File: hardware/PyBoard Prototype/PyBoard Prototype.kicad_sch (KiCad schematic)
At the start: 10 parts, among them J1 MIDI In, J2 MIDI Out, Q1 Q_PNP_BCE, U1 PyBoard_v1.1, U2 PC817, U3 MIKROE-506

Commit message: Some more experiments with MicroPython
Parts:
- added D?: D, symbol Device:D
- Q1: value Q_PNP_BCE -> 2N5401
- R2: value 150 -> 100
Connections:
- net +3V3: now also D?.2 (A); no longer R2.2
- new net: D?.1 (K), R2.2
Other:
- note added: "(3.3V - 0.6V) / 100Ohm = 27mA similar to 5V / 220Ohm from the MIDI specs, in case of short-circuit in the cable. However (5V-1.2V)/(2x220Ohm) = 8.6mA While (3V-0.6V-1.2V)/(100Ohm + 220Ohm) = 4.7mA Need to test if this is still sufficient."
- note removed: "3.3V / 150Ohm = 22mA similar to 5V / 220Ohm from the MIDI specs, in case of short-circuit in the cable. However (5V-1.2V)/(2x220Ohm) = 8.6mA While (3V-1.2v)/(150Ohm + 220Ohm) = 5.6mA Need to test if this is still sufficient. Otherwise 30Ohm would come close but draw 110mA in case of a short-circuit!"
- moved on the sheet: J2, Q1, R2

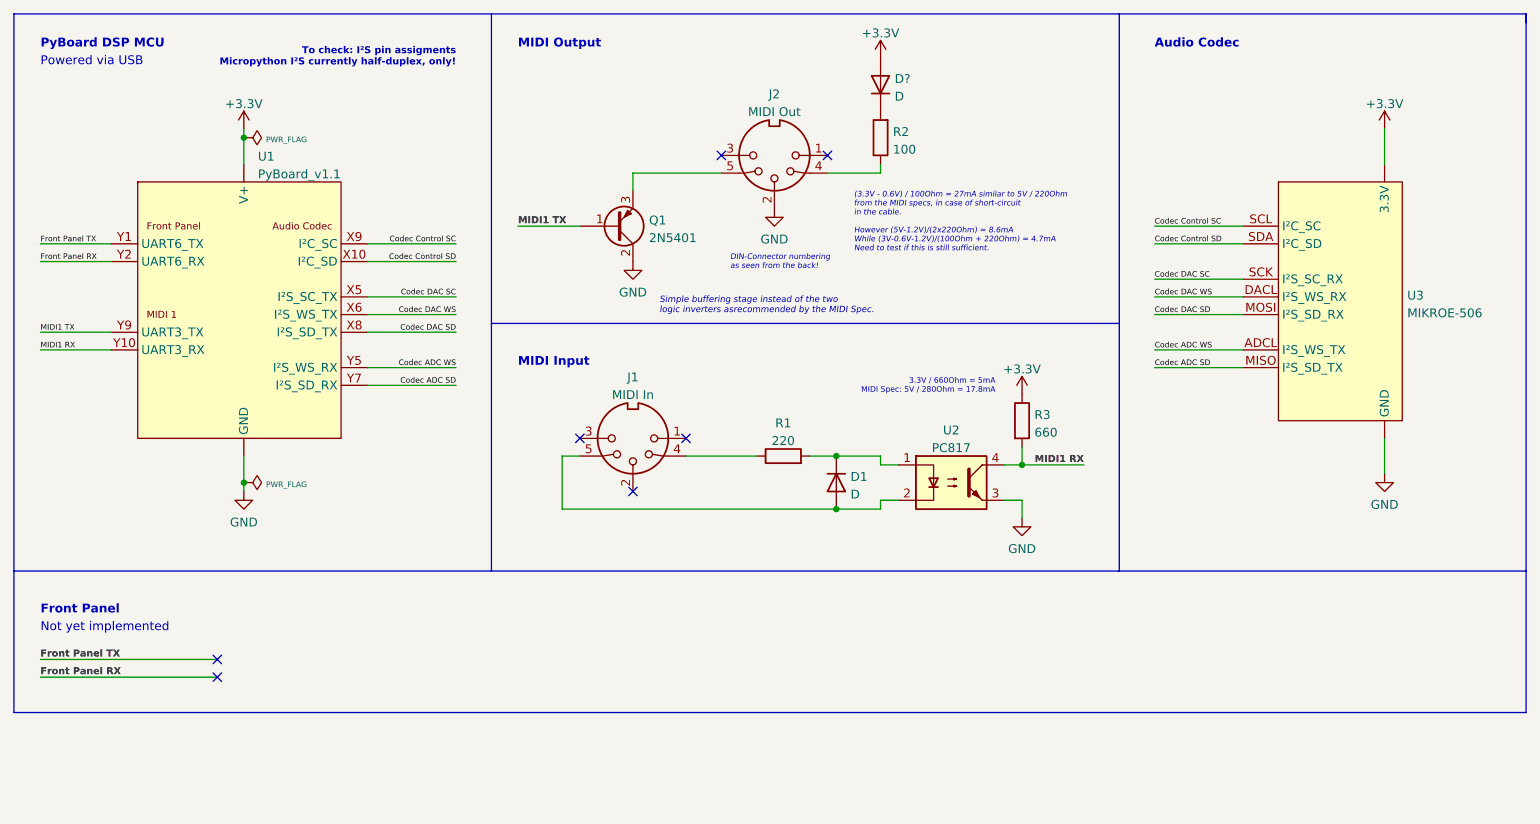
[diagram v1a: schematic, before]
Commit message: research/micropython/midi-in-out: More complex use case
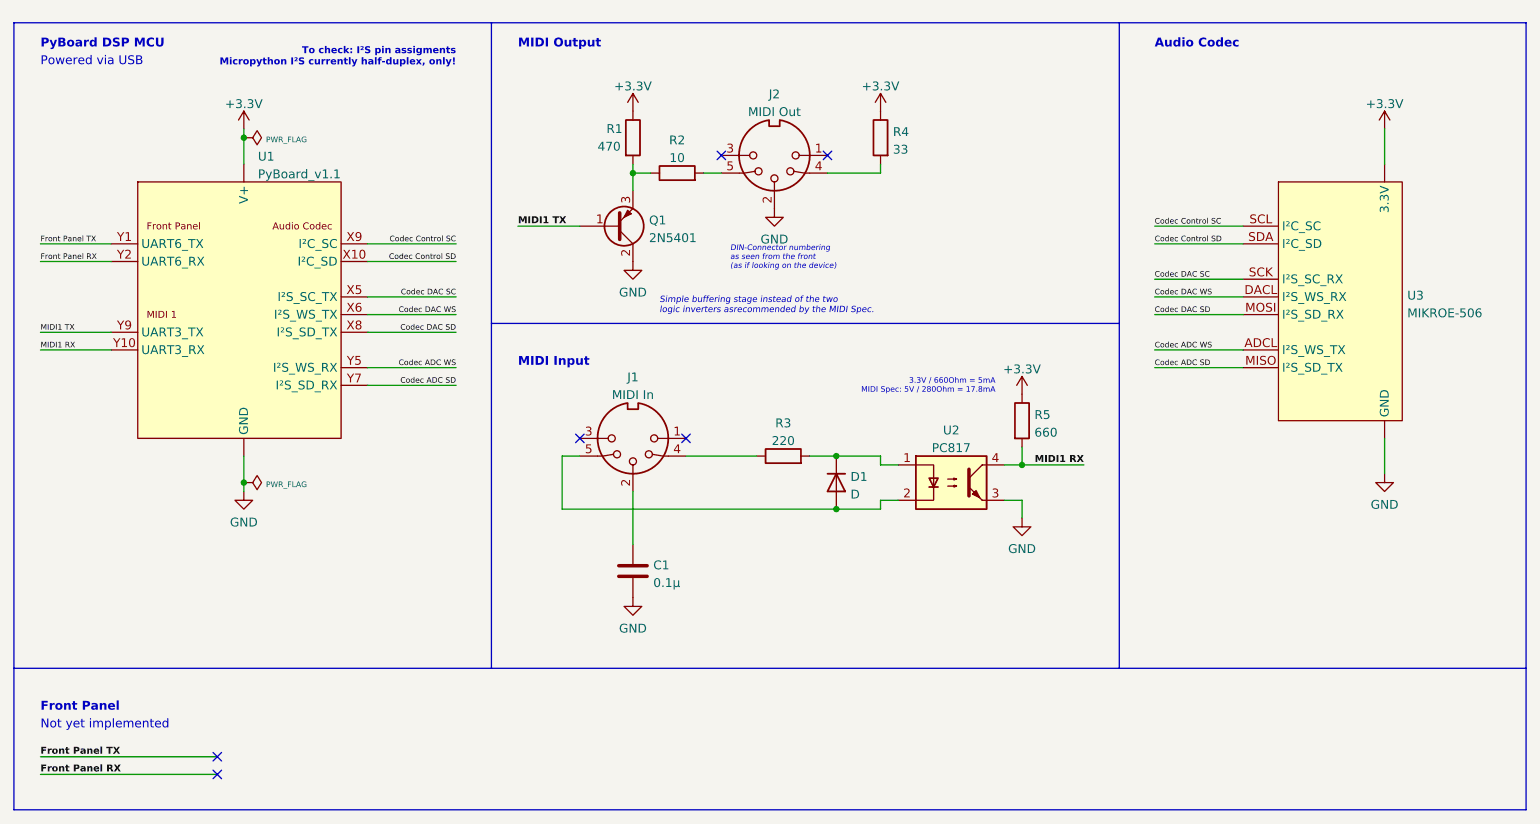
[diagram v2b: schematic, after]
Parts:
- removed D?: D, symbol Device:D
- added C1: 0.1µ, symbol Device:C
- added R1: 470, symbol Device:R
- added R2: 10, symbol Device:R
- R4: renamed from R2; value 100 -> 33
- renumbered R1 to R3, R3 to R5
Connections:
- net +3V3: now also R4.1, R1.1
- net GND: now also C1.2
- net at R4.2: now also J2.4
- net at Q1.3 (E): now also R1.2, R2.1; no longer J2.5
- net at J1.2: now also C1.1
- new net: J2.5, R2.2
- no-connect marks 7 -> 6
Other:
- note added: "DIN-Connector numbering as seen from the front (as if looking on the device)"
- note removed: "(3.3V - 0.6V) / 100Ohm = 27mA similar to 5V / 220Ohm from the MIDI specs, in case of short-circuit in the cable. However (5V-1.2V)/(2x220Ohm) = 8.6mA While (3V-0.6V-1.2V)/(100Ohm + 220Ohm) = 4.7mA Need to test if this is still sufficient."
- note removed: "DIN-Connector numbering as seen from the back!"
- moved on the sheet: R4
